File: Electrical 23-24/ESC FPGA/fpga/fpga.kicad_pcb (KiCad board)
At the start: 2 copper layers, 7.5 x 7.5 mm, 164 parts, among them J1 SBH11-PBPC-D07-ST-BK, J2 LSHM-110-04.0-L-DV-A-N-K-TR, J3 USB_B_Micro, J4 LSHM-110-04.0-L-DV-A-N-K-TR, J5 Conn_02x06_Top_Bottom, J6 Conn_02x06_Top_Bottom, J7 Conn_02x20_Odd_Even, J8 Conn_02x06_Top_Bottom, SW1 SW_SPDT, SW10 SW_SPDT, SW11 SW_SPDT, SW2 SW_Push, SW3 SW_SPDT, SW4 SW_SPDT, SW5 SW_SPDT, SW6 SW_Push, SW7 SW_Push, SW8 SW_Push, SW9 SW_SPDT, U1 XC6SLX9-TQG144, U12 MIC28515T-E/PHA, U13 FXMA108BQX, U14 FXMA108BQX, U15 FXMA108BQX, U5 MT25QL128ABA1ESE, U6 MIC28515T-E/PHA, U7 MIC28515T-E/PHA, U8 LM74700QDBVRQ1, U9 LM74700QDBVRQ1, X1 KC5032Z100.000C1JX00

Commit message: Finish groupings on FPGA PCB
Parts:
- added JP1: SolderJumper_2_Bridged, Jumper:SolderJumper-2_P1.3mm_Bridged2Bar_RoundedPad1.0x1.5mm, F.Cu at (24.6, 114.8)
- added JP2: SolderJumper_2_Bridged, Jumper:SolderJumper-2_P1.3mm_Bridged2Bar_RoundedPad1.0x1.5mm, F.Cu at (39.7, 114.6)
- added JP3: SolderJumper_2_Bridged, Jumper:SolderJumper-2_P1.3mm_Bridged2Bar_RoundedPad1.0x1.5mm, F.Cu at (56.5, 114.3)
- added JP4: SolderJumper_2_Bridged, Jumper:SolderJumper-2_P1.3mm_Bridged2Bar_RoundedPad1.0x1.5mm, F.Cu at (48.4, 62.9)
- added JP5: SolderJumper_2_Bridged, Jumper:SolderJumper-2_P1.3mm_Bridged2Bar_RoundedPad1.0x1.5mm, F.Cu at (33.4, 60.1)
- added JP6: SolderJumper_2_Bridged, Jumper:SolderJumper-2_P1.3mm_Bridged2Bar_RoundedPad1.0x1.5mm, F.Cu at (43.7, 53.9)
- added JP7: SolderJumper_2_Bridged, Jumper:SolderJumper-2_P1.3mm_Bridged2Bar_RoundedPad1.0x1.5mm, F.Cu at (38.2, 60.0)
- added JP8: SolderJumper_2_Bridged, Jumper:SolderJumper-2_P1.3mm_Bridged2Bar_RoundedPad1.0x1.5mm, F.Cu at (43.6, 65.2)
- added JP9: SolderJumper_2_Bridged, Jumper:SolderJumper-2_P1.3mm_Bridged2Bar_RoundedPad1.0x1.5mm, F.Cu at (39.4, 68.8)
- added REF**: RASPI, fpga:RASPI, F.Cu at (138.6, 43.3)
- C2: value 10u -> 4.7u; moved to B.Cu
- C47, C51: value 47u HV -> 1u HV
- D1, J7, R10, R11, R3, R35, R36, R37, R38, R39, R40, R41, R42, R43, R44, R45, R46, R47, R48, R49, R53, R54, R55, R9, U1: moved to B.Cu
- R1, R15, R22: value 1.42k -> 1.5k
- R12: value 10 -> 2.2
- R2, R5: value 4k7 -> 4.7k; moved to B.Cu
- R4: value 220 -> 330; moved to B.Cu
- R6: value 2k4 -> 2.2k
- moved C13 167.4 mm to (43.6, 56.9), turned to 180 degrees
- moved C12 166.0 mm to (43.6, 57.9), turned to 180 degrees
- moved C11 164.8 mm to (43.6, 58.8), turned to 180 degrees
- moved C10 163.5 mm to (43.6, 59.7), turned to 180 degrees
- moved C5 163.1 mm to (38.2, 64.5)
- moved C9 162.8 mm to (43.6, 60.7), turned to 180 degrees
- moved C4 162.7 mm to (38.2, 63.6)
- moved C3 162.2 mm to (38.2, 62.6)
- moved C1 161.8 mm to (38.2, 61.7)
- moved C8 161.5 mm to (43.6, 61.6), turned to 180 degrees
- moved C7 160.3 mm to (43.6, 62.5), turned to 180 degrees
- moved C6 159.0 mm to (43.6, 63.5), turned to 180 degrees
- moved R3 158.5 mm to (51.2, 48.6), turned to 180 degrees
- moved R4 157.2 mm to (52.3, 51.6), turned to 180 degrees
- moved D2 155.1 mm to (24.2, 105.7), turned to -90 degrees
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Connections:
- C1 pad 1: 1V2 -> VCC_INT
- C10 pad 1: 3V3 -> VCC_AUX
- C11 pad 1: 3V3 -> VCC_AUX
- C12 pad 1: 3V3 -> VCC_AUX
- C13 pad 1: 3V3 -> VCC_AUX
- C17 pad 1: 3V3 -> VCCO_1
- C18 pad 1: 3V3 -> VCCO_1
- C19 pad 1: 3V3 -> VCCO_1
- C20 pad 1: 3V3 -> VCCO_2
- C21 pad 1: 3V3 -> VCCO_2
- C22 pad 1: 3V3 -> VCCO_2
- C23 pad 1: 3V3 -> VCCO_3
- C24 pad 1: 3V3 -> VCCO_3
- C25 pad 1: 3V3 -> VCCO_3
- C3 pad 1: 1V2 -> VCC_INT
- C32 pad 1: GND -> GNDA
- C35 pad 2: GND -> GNDA
- C4 pad 1: 1V2 -> VCC_INT
- C41 pad 1: GND -> GNDA
- C45 pad 2: GND -> GNDA
- C5 pad 1: 1V2 -> VCC_INT
- C58 pad 1: GND -> GNDA
- C6 pad 1: 3V3 -> VCC_AUX
- C61 pad 1: /Regulators/2V5 -> 2V5
- C62 pad 1: /Regulators/2V5 -> 2V5
- C62 pad 2: GND -> GNDA
- C7 pad 1: 3V3 -> VCC_AUX
- C8 pad 1: 3V3 -> VCC_AUX
- C9 pad 1: 3V3 -> VCC_AUX
- D2 pad 2: /Regulators/2V5 -> 2V5
- D3 pad 2: /Regulators/2V5 -> 2V5
- D4 pad 2: /Regulators/2V5 -> 2V5
- J1 pad 2: 3V3 -> VCC_AUX
- L3 pad 2: /Regulators/2V5 -> 2V5
- LED1 pad 3: 3V3 -> VCCO_2
- LED2 pad 3: 3V3 -> VCCO_2
- LED3 pad 3: 3V3 -> VCCO_2
- LED4 pad 3: 3V3 -> VCCO_2
- R10 pad 1: 3V3 -> VCCO_2
- R13 pad 1: 3V3 -> VCCO_2
- R14 pad 1: 3V3 -> VCCO_2
- R2 pad 1: 3V3 -> VCCO_2
- R21 pad 2: GND -> GNDA
- R28 pad 2: GND -> GNDA
- R3 pad 2: 3V3 -> VCCO_2
- R33 pad 1: /Regulators/2V5 -> 2V5
- R34 pad 2: GND -> GNDA
- R47 pad 2: 3V3 -> VCCO_2
- R48 pad 2: 3V3 -> VCCO_2
- R49 pad 2: 3V3 -> VCCO_2
- R5 pad 1: 3V3 -> VCCO_2
- R50 pad 2: 3V3 -> VCCO_2
- R51 pad 2: 3V3 -> VCCO_3
- R52 pad 2: 3V3 -> VCCO_3
- R6 pad 1: 3V3 -> VCCO_2
- R8 pad 2: 3V3 -> VCCO_2
- SW1 pad 1: /Regulators/2V5 -> 2V5
- SW1 pad 2: VCCO_0 -> Net-(JP9-B)
- U1 pad 103: 3V3 -> VCCO_1
- U1 pad 128: 1V2 -> VCC_INT
- U1 pad 129: 3V3 -> VCC_AUX
- U1 pad 18: 3V3 -> VCCO_3
- U1 pad 19: 1V2 -> VCC_INT
- U1 pad 20: 3V3 -> VCC_AUX
- U1 pad 28: 1V2 -> VCC_INT
- U1 pad 31: 3V3 -> VCCO_3
- U1 pad 36: 3V3 -> VCC_AUX
- U1 pad 4: 3V3 -> VCCO_3
- U1 pad 42: 3V3 -> VCCO_2
- U1 pad 52: 1V2 -> VCC_INT
- U1 pad 53: 3V3 -> VCC_AUX
- U1 pad 63: 3V3 -> VCCO_2
- U1 pad 76: 3V3 -> VCCO_1
- U1 pad 86: 3V3 -> VCCO_1
- U1 pad 89: 1V2 -> VCC_INT
- U1 pad 90: 3V3 -> VCC_AUX
- U12 pad 28: GND -> GNDA
- U5 pad 8: 3V3 -> VCCO_2
- U6 pad 28: GND -> GNDA
- U7 pad 28: GND -> GNDA
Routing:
- net GND: track 0.00 -> 219.0 mm, vias 0 -> 5
- net GNDA: track 0.00 -> 79.2 mm, vias 0 -> 12
- net /Regulators/VIN: track 0.00 -> 63.2 mm, vias 0 -> 42
- net /Regulators/FB3: track 0.00 -> 19.8 mm, vias 0 -> 2
- net /Regulators/FB1: track 0.00 -> 19.8 mm, vias 0 -> 2
- net /Regulators/FB2: track 0.00 -> 19.8 mm, vias 0 -> 2
- net 3V3: track 0.00 -> 14.8 mm, vias 0 -> 7
- net VCCO_2: track 0.00 -> 14.3 mm, vias 0 -> 4
- net VUSB: track 0.00 -> 14.2 mm
- net /Regulators/SW2: track 0.00 -> 13.9 mm, vias 0 -> 4
- net /Regulators/SW1: track 0.00 -> 13.9 mm, vias 0 -> 4
- net /Regulators/SW3: track 0.00 -> 13.9 mm, vias 0 -> 4
- net VBATT: track 0.00 -> 13.7 mm
- net VCC_AUX: track 0.00 -> 8.29 mm
- net Net-(U6-PVDD): track 0.00 -> 6.86 mm, vias 0 -> 2
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- added copper zone on F.Cu, net /Regulators/SW1
- added copper zone on F.Cu, net /Regulators/VIN
- added copper zone on F.Cu, net 1V2
- added copper zone on F.Cu, net 2V5
- added copper zone on F.Cu, net 3V3
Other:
- board size 7.5 x 7.5 mm -> 52 x 20.7 mm

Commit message: Finished hard signal routing, need PMOD and Power
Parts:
- C26, C27, C28, C29, C30, C31, C32, C33, C34, C35, C36, C37, C38, C39, C40, C41, C42, C43, C44, C45, C46, C47, C48, C49, C50, C51, C52, C53, C54, C55, C56, C57, C58, C59, C60, C61, C62, D2, D3, D4, JP1, JP2, JP3, L1, L2, L3, R1, R12, R13, R14, R15, R16, R17, R18, R19, R20, R21, R22, R23, R24, R25, R26, R27, R28, R29, R30, R31, R32, R33, R34, R50, R51, R52, R56, R57, R58, R6, R7, R8, U10, U11, U12, U13, U14, U15, U5, U6, U7, U8, U9, X1: moved to B.Cu
- D1, R10, R11, R3, R4, R5, R9: moved to F.Cu
- moved R47 199.6 mm to (71.6, 68.7)
- moved R53 199.6 mm to (76.7, 76.3)
- moved SW6 199.6 mm to (76.7, 74.2)
- moved R49 199.0 mm to (71.6, 45.7)
- moved R55 199.0 mm to (76.6, 53.4)
- moved SW8 199.0 mm to (76.6, 51.3)
- moved SW11 175.9 mm to (85.1, 56.3)
- moved R58 175.4 mm to (83.8, 58.3)
- moved R52 175.0 mm to (83.8, 62.0)
- moved SW10 169.2 mm to (81.5, 56.3)
- moved R57 168.7 mm to (80.2, 58.3)
- moved R51 168.3 mm to (80.2, 62.0)
- moved SW9 164.3 mm to (77.9, 56.3)
- moved R56 163.8 mm to (76.6, 58.3)
- moved R50 163.4 mm to (76.6, 62.0)
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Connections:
- J2 pad 02: Net-(U1A-IO_L1N_VREF_0) -> Net-(U1A-IO_L35P_GCLK17_0)
- J2 pad 04: Net-(U1A-IO_L2P_0) -> Net-(U1A-IO_L34N_GCLK18_0)
- J2 pad 06: Net-(U1A-IO_L2N_0) -> Net-(U1A-IO_L34P_GCLK19_0)
- J2 pad 08: Net-(U1A-IO_L3P_0) -> Net-(U1A-IO_L4N_0)
- J2 pad 10: Net-(U1A-IO_L3N_0) -> Net-(U1A-IO_L4P_0)
- J2 pad 12: Net-(U1A-IO_L4P_0) -> Net-(U1A-IO_L3N_0)
- J2 pad 14: Net-(U1A-IO_L4N_0) -> Net-(U1A-IO_L3P_0)
- J2 pad 16: Net-(U1A-IO_L34P_GCLK19_0) -> Net-(U1A-IO_L2N_0)
- J2 pad 18: Net-(U1A-IO_L34N_GCLK18_0) -> Net-(U1A-IO_L2P_0)
- J2 pad 20: Net-(U1A-IO_L35P_GCLK17_0) -> Net-(U1A-IO_L1N_VREF_0)
- J4 pad 02: Net-(U1A-IO_L37N_GCLK12_0) -> Net-(U1A-IO_L66P_SCP1_0)
- J4 pad 04: Net-(U1A-IO_L62P_0) -> Net-(U1A-IO_L65N_SCP2_0)
- J4 pad 06: Net-(U1A-IO_L62N_VREF_0) -> Net-(U1A-IO_L65P_SCP3_0)
- J4 pad 08: Net-(U1A-IO_L63P_SCP7_0) -> Net-(U1A-IO_L64N_SCP4_0)
- J4 pad 10: Net-(U1A-IO_L63N_SCP6_0) -> Net-(U1A-IO_L64P_SCP5_0)
- J4 pad 12: Net-(U1A-IO_L64P_SCP5_0) -> Net-(U1A-IO_L63N_SCP6_0)
- J4 pad 13: Net-(U1A-IO_L47N_1) -> Net-(U1A-IO_L74N_DOUT_BUSY_1)
- J4 pad 14: Net-(U1A-IO_L64N_SCP4_0) -> Net-(U1A-IO_L63P_SCP7_0)
- J4 pad 16: Net-(U1A-IO_L65P_SCP3_0) -> Net-(U1A-IO_L62N_VREF_0)
- J4 pad 17: Net-(U1A-IO_L74N_DOUT_BUSY_1) -> Net-(U1A-IO_L47N_1)
- J4 pad 18: Net-(U1A-IO_L65N_SCP2_0) -> Net-(U1A-IO_L62P_0)
- J4 pad 20: Net-(U1A-IO_L66P_SCP1_0) -> Net-(U1A-IO_L37N_GCLK12_0)
- J8 pad 10: 2V5 -> 1V2
- J8 pad 11: 1V2 -> GND
- J8 pad 2: VUSB -> VBATT
- J8 pad 3: 3V3 -> VUSB
- J8 pad 4: 2V5 -> VUSB
- J8 pad 5: 1V2 -> 3V3
- J8 pad 6: GND -> 3V3
- J8 pad 7: VBATT -> 2V5
- J8 pad 8: VUSB -> 2V5
- J8 pad 9: 3V3 -> 1V2
- U1 pad 101: GPIO27 -> GPIO16
- U1 pad 102: GPIO26 -> GPIO12
- U1 pad 104: GPIO25 -> GPIO20
- U1 pad 105: GPIO24 -> GPIO21
- U13 pad 12: GPIO7 -> GPIO22
- U13 pad 13: GPIO6 -> GPIO23
- U13 pad 14: GPIO5 -> GPIO9
- U13 pad 15: GPIO3 -> GPIO24
- U13 pad 16: GPIO4 -> GPIO25
- U13 pad 17: GPIO2 -> GPIO8
- U13 pad 18: GPIO1 -> GPIO7
- U13 pad 19: GPIO0 -> GPIO10
- U14 pad 12: GPIO15 -> GPIO11
- U14 pad 13: GPIO14 -> GPIO0
- U14 pad 14: GPIO11 -> GPIO5
- U14 pad 15: GPIO12 -> GPIO6
- U14 pad 16: GPIO13 -> GPIO1
- U14 pad 17: GPIO10 -> GPIO13
- U14 pad 18: GPIO9 -> GPIO19
- U14 pad 19: GPIO8 -> GPIO26
- U15 pad 12: GPIO18 -> GPIO2
- U15 pad 13: GPIO22 -> GPIO4
- U15 pad 14: GPIO21 -> GPIO3
- U15 pad 15: GPIO20 -> GPIO14
- U15 pad 16: GPIO19 -> GPIO15
- U15 pad 17: GPIO23 -> GPIO17
- U15 pad 18: GPIO17 -> GPIO18
- U15 pad 19: GPIO16 -> GPIO27
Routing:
- net GND: track 219.0 -> 359.0 mm, vias 5 -> 29
- net GPIO12: track 0.00 -> 70.0 mm, vias 0 -> 2
- net GPIO21: track 0.00 -> 63.4 mm, vias 0 -> 3
- net GPIO16: track 0.00 -> 62.8 mm, vias 0 -> 2
- net GPIO20: track 0.00 -> 60.6 mm, vias 0 -> 1
- net GPIO23: track 0.00 -> 56.4 mm
- net GPIO24: track 0.00 -> 56.3 mm
- net GPIO22: track 0.00 -> 54.4 mm, vias 0 -> 1
- net GPIO1: track 0.00 -> 54.2 mm, vias 0 -> 2
- net GPIO10: track 0.00 -> 53.4 mm, vias 0 -> 1
- net GPIO25: track 0.00 -> 52.7 mm, vias 0 -> 1
- net VCC_AUX: track 8.29 -> 59.9 mm, vias 0 -> 5
- net GPIO8: track 0.00 -> 51.4 mm
- net GPIO11: track 0.00 -> 51.3 mm, vias 0 -> 1
- net GPIO7: track 0.00 -> 50.0 mm, vias 0 -> 1
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- added copper zone on B.Cu, net /Regulators/SW1
- added copper zone on B.Cu, net /Regulators/VIN
- added copper zone on B.Cu, net 1V2
- added copper zone on B.Cu, net 2V5
- added copper zone on B.Cu, net 3V3
- removed copper zone on F.Cu, net /Regulators/SW1
- removed copper zone on F.Cu, net /Regulators/VIN
- removed copper zone on F.Cu, net 1V2
- removed copper zone on F.Cu, net 2V5
- removed copper zone on F.Cu, net 3V3
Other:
- board size 52 x 20.7 mm -> 85 x 56 mm

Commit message: Finish PCB layout, need to DRC
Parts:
- moved R48 3.13 mm to (84.0, 66.0), turned to 90 degrees
- moved R2 0.88 mm to (93.0, 51.6)
- moved SW3 0.86 mm to (137.0, 53.3)
- moved R58 0.54 mm to (83.8, 58.8)
- moved R57 0.53 mm to (80.2, 58.8)
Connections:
- J5 pad 10: PMOD1_7 -> GND
- J5 pad 11: GND -> 3V3
- J5 pad 2: PMOD1_1 -> PMOD1_4
- J5 pad 3: PMOD1_2 -> PMOD1_1
- J5 pad 4: PMOD1_3 -> PMOD1_5
- J5 pad 5: GND -> PMOD1_2
- J5 pad 6: 3V3 -> PMOD1_6
- J5 pad 7: PMOD1_4 -> PMOD1_3
- J5 pad 8: PMOD1_5 -> PMOD1_7
- J5 pad 9: PMOD1_6 -> GND
- J6 pad 10: PMOD2_7 -> GND
- J6 pad 11: GND -> 3V3
- J6 pad 2: PMOD2_1 -> PMOD2_4
- J6 pad 3: PMOD2_2 -> PMOD2_1
- J6 pad 4: PMOD2_3 -> PMOD2_5
- J6 pad 5: GND -> PMOD2_2
- J6 pad 6: 3V3 -> PMOD2_6
- J6 pad 7: PMOD2_4 -> PMOD2_3
- J6 pad 8: PMOD2_5 -> PMOD2_7
- J6 pad 9: PMOD2_6 -> GND
- REF** pad 1: (no net) -> GND
- U1 pad 15: PMOD1_5 -> PMOD1_2
- U1 pad 16: PMOD1_4 -> PMOD1_5
- U1 pad 17: PMOD1_2 -> PMOD1_1
- U1 pad 2: PMOD2_6 -> PMOD2_3
- U1 pad 21: PMOD1_1 -> PMOD1_4
- U1 pad 34: /Bank2/SW3 -> /Bank2/SW2
- U1 pad 35: /Bank2/SW2 -> /Bank2/SW3
- U1 pad 5: PMOD2_5 -> PMOD2_6
- U1 pad 6: PMOD2_4 -> PMOD2_2
- U1 pad 7: PMOD2_3 -> PMOD2_5
- U1 pad 8: PMOD2_2 -> PMOD2_1
- U1 pad 9: PMOD2_1 -> PMOD2_4
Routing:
- net GND: track 359.0 -> 920.2 mm, vias 29 -> 121
- net 3V3: track 27.7 -> 295.3 mm, vias 9 -> 37
- net VUSB: track 34.5 -> 256.7 mm, vias 2 -> 17
- net VBATT: track 17.3 -> 203.6 mm, vias 0 -> 13
- net 1V2: track 0.07 -> 120.1 mm, vias 7 -> 18
- net 2V5: track 0.07 -> 119.9 mm, vias 10 -> 16
- net /Regulators/VIN: track 61.9 -> 175.3 mm, vias 42 -> 45
- net VCCO_2: track 35.6 -> 147.6 mm, vias 6 -> 16
- net PMOD1_5: track 0.00 -> 61.9 mm, vias 0 -> 2
- net PMOD1_1: track 0.00 -> 56.7 mm, vias 0 -> 2
- net /Bank2/BTN1: track 1.51 -> 58.0 mm, vias 0 -> 2
- net OE: track 0.00 -> 55.9 mm, vias 0 -> 4
- net PMOD1_4: track 0.00 -> 55.9 mm
- net PMOD1_2: track 0.00 -> 53.1 mm, vias 0 -> 2
- net /Bank2/BTN3: track 1.54 -> 54.6 mm, vias 0 -> 5
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- added copper zone on F.Cu, net /Regulators/VIN
- added copper zone on F.Cu, net 1V2
- added copper zone on F.Cu, net 2V5
- added copper zone on F.Cu, net 3V3
- added copper zone on B.Cu, net GND
- added copper zone on F.Cu, net GND

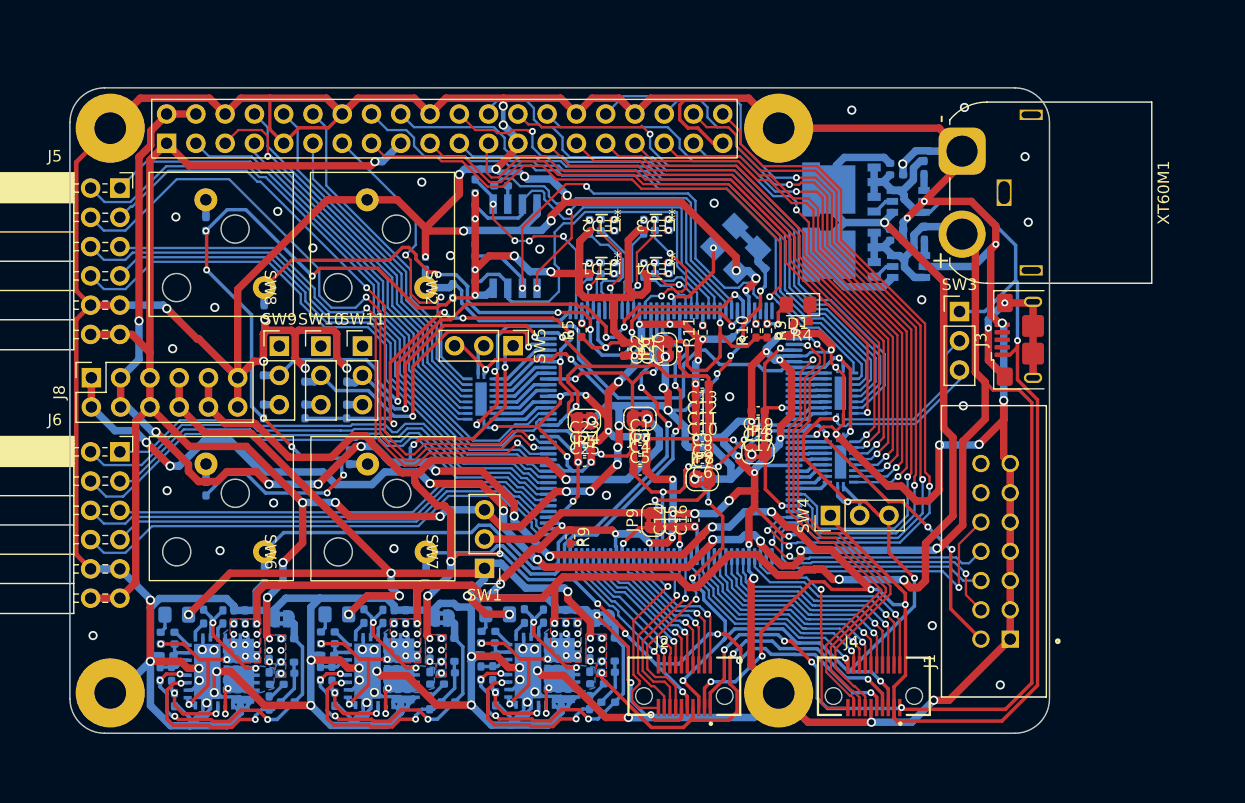
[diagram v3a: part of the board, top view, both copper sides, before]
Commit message: Turn XT60
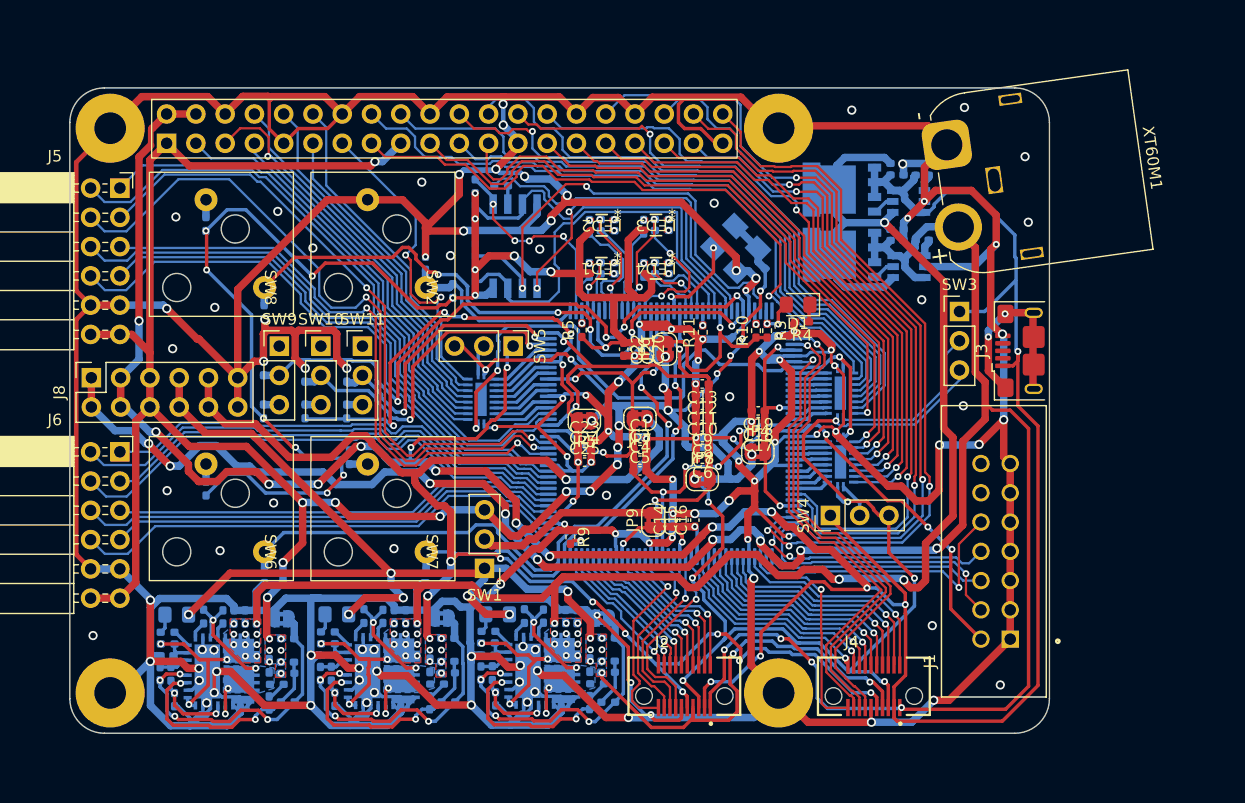
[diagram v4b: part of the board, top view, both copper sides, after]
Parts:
- removed REF**: RASPI, fpga:RASPI
- added J9: Conn_01x01_Pin, fpga:RASPI, F.Cu at (59.8, 33.9)
- moved XT60M1 1.43 mm to (135.9, 38.9), turned to -82 degrees
- moved J3 0.96 mm to (143.4, 56.8)
- moved C50 0.68 mm to (133.7, 41.5), turned to 0 degrees
- moved C48 0.64 mm to (133.7, 47.2), turned to 0 degrees
- moved R17 0.06 mm to (68.5, 84.8)
- moved R23 0.05 mm to (82.4, 84.8)
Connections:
- C32 pad 1: GNDA -> GND1
- C35 pad 2: GNDA -> GND1
- C41 pad 1: GNDA -> GND2
- C45 pad 2: GNDA -> GND2
- C58 pad 1: GNDA -> GND3
- C62 pad 2: GNDA -> GND3
- JP1 pad 1: GNDA -> GND1
- JP2 pad 1: GNDA -> GND2
- JP3 pad 1: GNDA -> GND3
- R21 pad 2: GNDA -> GND1
- R28 pad 2: GNDA -> GND2
- R34 pad 2: GNDA -> GND3
- U12 pad 28: GNDA -> GND3
- U6 pad 28: GNDA -> GND1
- U7 pad 28: GNDA -> GND2
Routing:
- net GNDA: track 79.2 -> 0.00 mm, vias 12 -> 0
- net GND3: track 0.00 -> 26.6 mm, vias 0 -> 4
- net GND2: track 0.00 -> 26.6 mm, vias 0 -> 4
- net GND1: track 0.00 -> 26.4 mm, vias 0 -> 4
- net GND: track 920.2 -> 913.5 mm
- net 3V3: track 295.3 -> 296.8 mm
- net VCCO_2: track 147.6 -> 148.7 mm
- net SPI_CLK: track 44.0 -> 42.9 mm
- net VCC_INT: track 55.5 -> 56.4 mm
- net /Regulators/SW1: track 14.4 -> 13.6 mm
- net OE: track 55.9 -> 56.8 mm
- net /Regulators/VIN: track 175.3 -> 176.0 mm
- net VCCO_3: track 55.2 -> 55.8 mm
- net VBATT: track 203.6 -> 203.0 mm
- added copper zone on B.Cu, net /Regulators/SW2
- added copper zone on B.Cu, net /Regulators/SW3
